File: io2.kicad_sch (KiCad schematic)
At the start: 59 parts, among them IC1 ILD217T, IC2 ILD217T, Q10 BC846, Q11 BC846, Q8 BC846, Q9 BC846, U11 74HC14, U12 74HC165, X3 Conn_DI

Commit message: Redesign PCB
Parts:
- added C13, C14: 100n, Capacitor_SMD:C_0603_1608Metric, symbol Device:C_Small
- added C29: 22µ, Capacitor_SMD:CP_Elec_4x5.8, symbol Device:C_Polarized_Small
- added JP5: DI_VCC, Jumper:SolderJumper-2_P1.3mm_Open_RoundedPad1.0x1.5mm, symbol Jumper:SolderJumper_2_Open
- added JP6: DI_GND, Jumper:SolderJumper-2_P1.3mm_Open_RoundedPad1.0x1.5mm, symbol Jumper:SolderJumper_2_Open
- added PS2: TEA 1-0505, Converter_DCDC:Converter_DCDC_Murata_MEE1SxxxxSC_THT, symbol Converter_DCDC:MEE1S0303SC
- added R56: n.b., Resistor_SMD:R_0603_1608Metric, symbol Device:R_Small
- D20, D21, D22, D23: footprint Package_TO_SOT_SMD:SOT-323_SC-70 -> Package_TO_SOT_SMD:SOT-23
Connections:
- net +3V3: now also U12.4 (D5)
- net +5V: now also C13.1, JP5.1 (A), PS2.2 (+Vin); no longer X3.5 (Pin_5), X3.6 (Pin_6)
- net DI2_P: now also X3.3 (Pin_3); no longer X3.2 (Pin_2)
- net DI3_P: now also X3.5 (Pin_5); no longer X3.3 (Pin_3)
- net DI4_P: now also X3.7 (Pin_7); no longer X3.4 (Pin_4)
- net GND: now also C13.2, JP6.1 (A), PS2.1 (-Vin); no longer U12.4 (D5), X3.8 (Pin_8), X3.9 (Pin_9)
- net GND1: now also X3.9 (Pin_9), C14.2, C29.2, JP6.2 (B), PS2.3 (-Vout), R56.1; no longer X3.7 (Pin_7)
- new net 5V_1: C14.1, C29.1, JP5.2 (B), PS2.4 (+Vout), R56.2, X3.2 (Pin_2), X3.4 (Pin_4), X3.6 (Pin_6), X3.8 (Pin_8)
- no-connect marks 1 -> 3
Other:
- note added: "Alternativbestückung: PS2 oder JP5,JP6"
- note added: "HW0"
- note added: "HW1"
- note added: "HW2"
- note added: "Reserve"
- note removed: "ToDo: BAT54 falscher Footprint"
- moved on the sheet: C27, U11E, U11F, U11G, X3

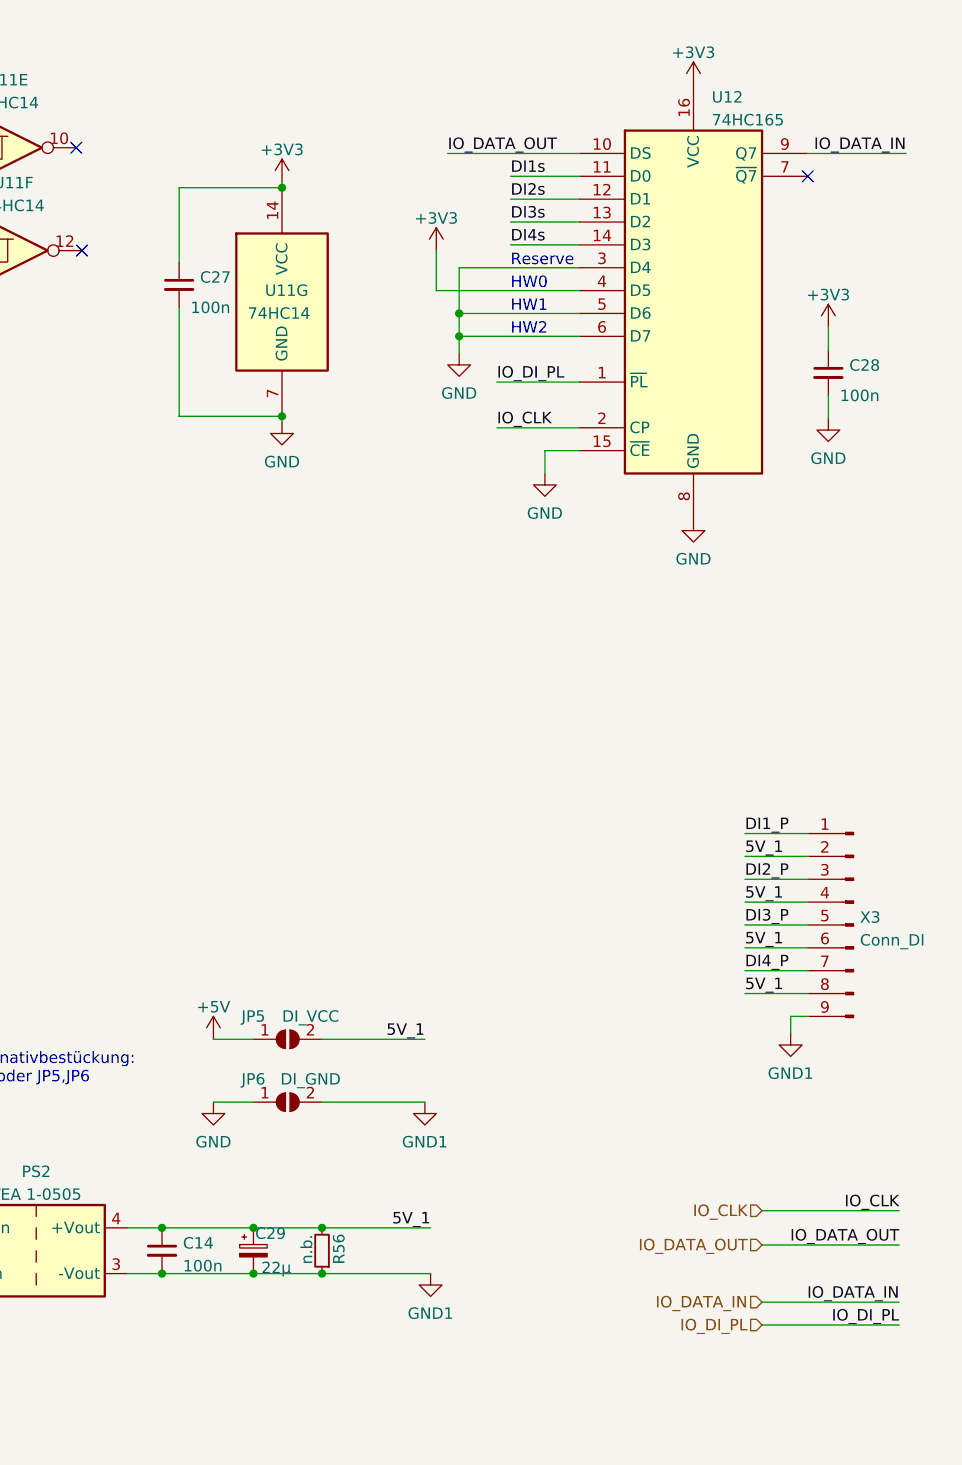
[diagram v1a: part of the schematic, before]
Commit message: Layout optimized
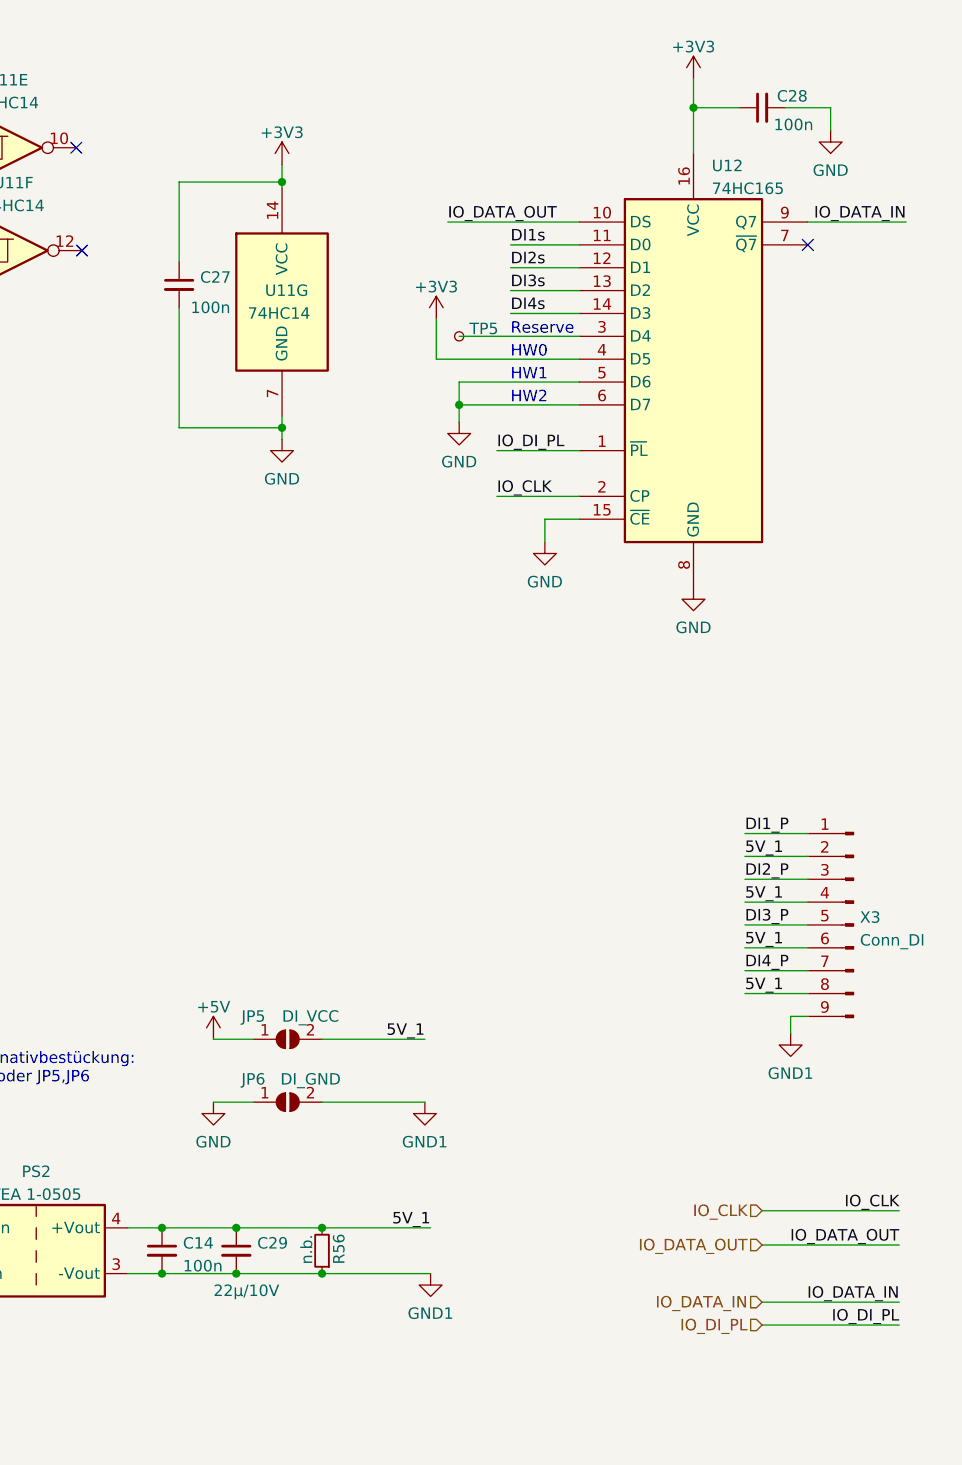
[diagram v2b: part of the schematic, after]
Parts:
- removed C29: 22µ, Capacitor_SMD:CP_Elec_4x5.8, symbol Device:C_Polarized_Small
- added C29: 22µ/10V, Capacitor_SMD:C_1206_3216Metric, symbol Device:C_Small
- added TP5: TP, TestPoint:TestPoint_Pad_1.0x1.0mm, symbol Connector:TestPoint_Small
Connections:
- net 5V_1: now also C29.1
- net GND: no longer U12.3 (D4)
- net GND1: now also C29.2
- new net: TP5.1, U12.3 (D4)
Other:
- moved on the sheet: C28, U12

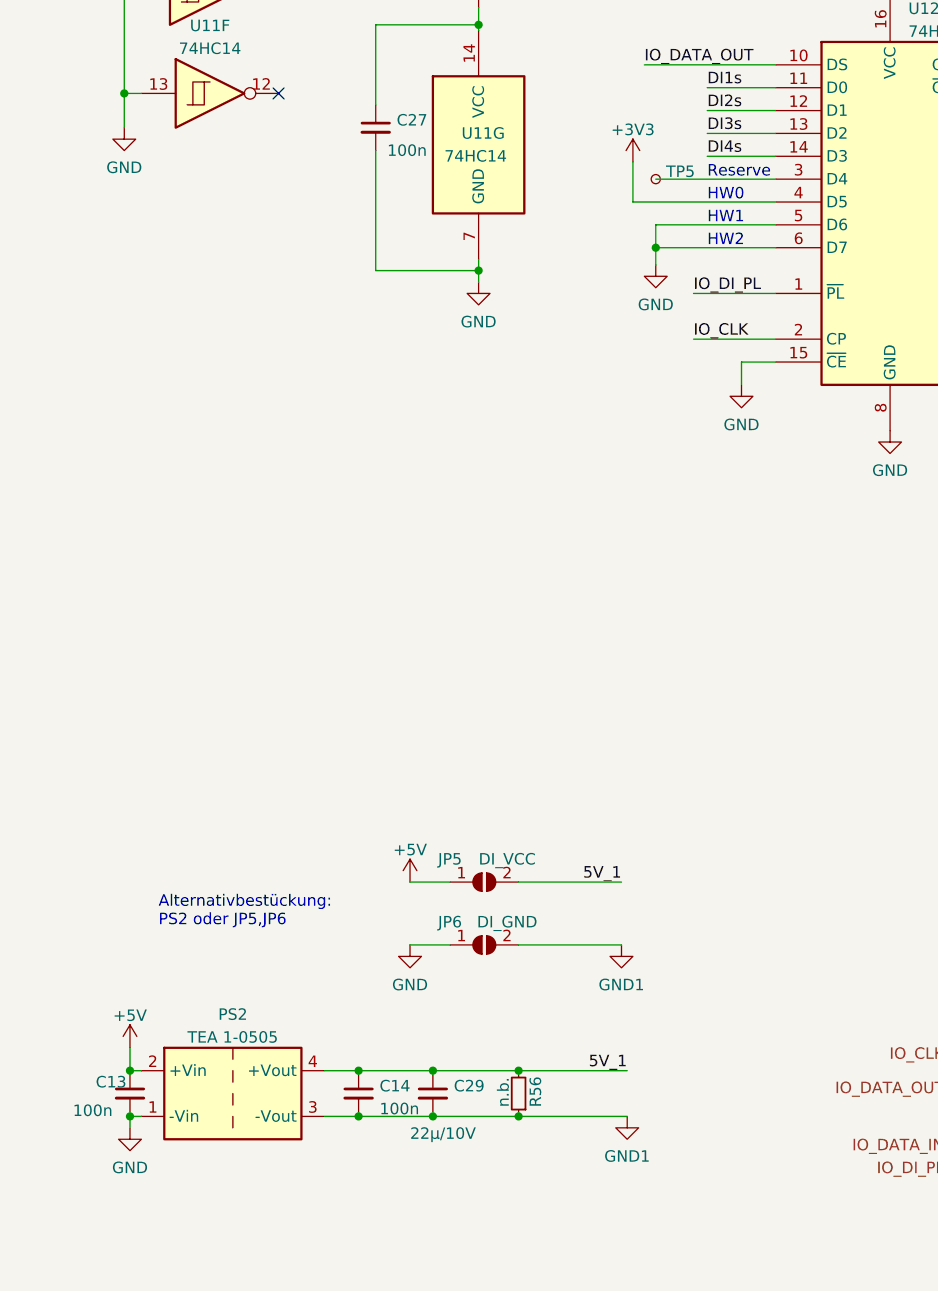
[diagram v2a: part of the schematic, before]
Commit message: Change extension bus
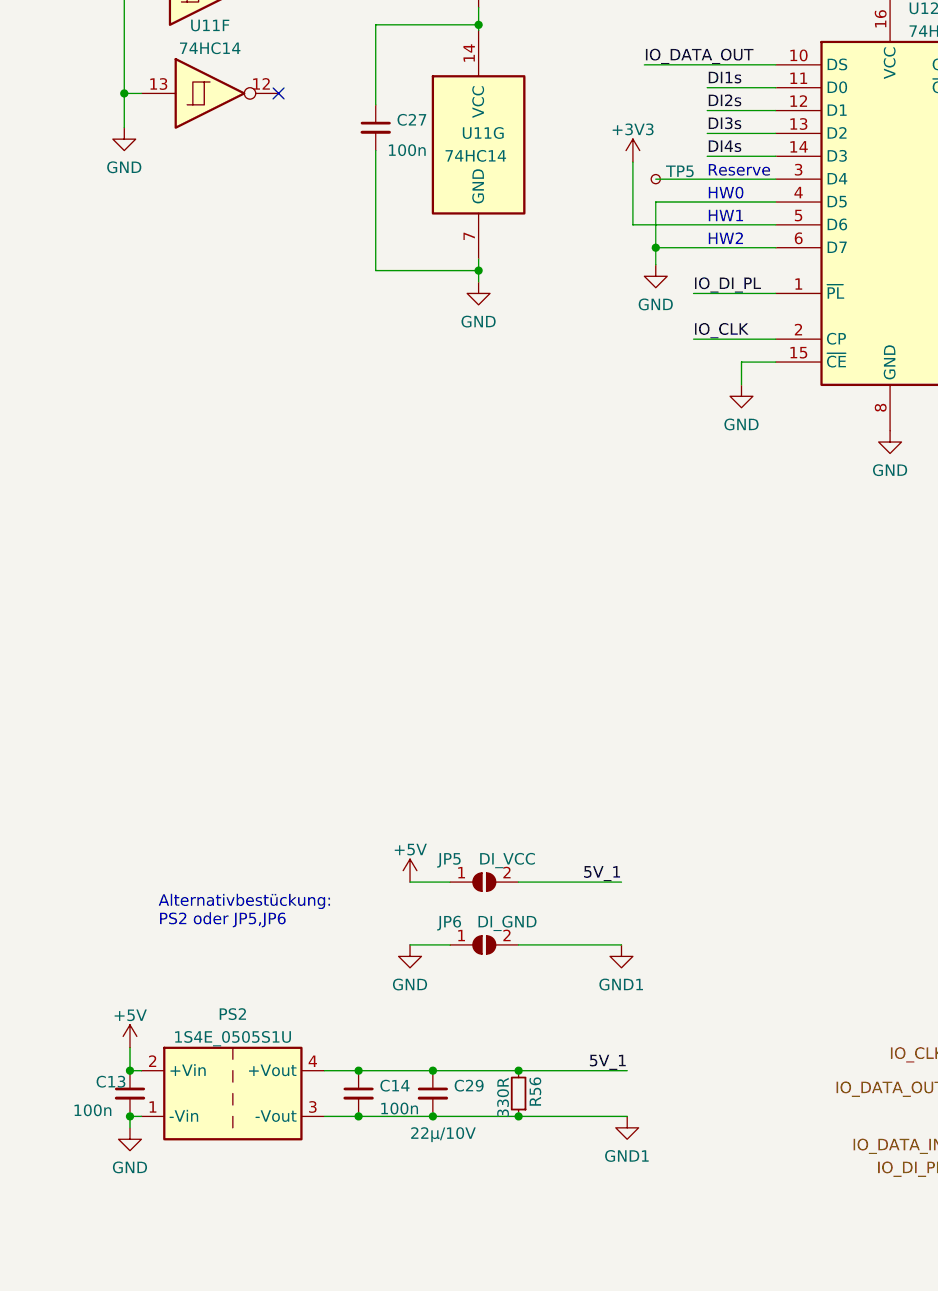
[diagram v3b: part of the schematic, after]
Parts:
- D20, D21, D22, D23: footprint Package_TO_SOT_SMD:SOT-23 -> Package_TO_SOT_SMD:SOT-323_SC-70
- IC1, IC2: footprint Package_SO:SOIC-8_5.23x5.23mm_P1.27mm -> Package_SO:SOIC-8_3.9x4.9mm_P1.27mm
- PS2: value TEA 1-0505 -> 1S4E_0505S1U; footprint Converter_DCDC:Converter_DCDC_Murata_MEE1SxxxxSC_THT -> custom_th:Converter_DCDC_GAPTEC_1S4E_S1U
- R56: value n.b. -> 330R
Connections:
- net +3V3: now also U12.5 (D6); no longer U12.4 (D5)
- net GND: now also U12.4 (D5); no longer U12.5 (D6)
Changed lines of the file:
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@@
   (title_block
     (title "BSC")
-    (date "2022-12-16")
-    (rev "2.1")
+    (date "2023-03-30")
+    (rev "2.3")
   )
   (junction (at 115.57 118.745) (diameter 0) (color 0 0 0 0)
@@
     (stroke (width 0) (type default) (color 0 0 0 0))
   )
-  (wire (pts (xy 227.33 48.26) (xy 227.33 52.705))
+  (wire (pts (xy 227.33 48.26) (xy 227.33 55.245))
     (stroke (width 0) (type default) (color 0 0 0 0))
   )
@@
     (stroke (width 0) (type default) (color 0 0 0 0))
   )
-  (wire (pts (xy 229.87 55.245) (xy 243.205 55.245))
-    (stroke (width 0) (type default) (color 0 0 0 0))
-  )
   (wire (pts (xy 145.415 132.08) (xy 151.765 132.08))
     (stroke (width 0) (type default) (color 0 0 0 0))
@@
     (stroke (width 0) (type default) (color 0 0 0 0))
   )
+  (wire (pts (xy 227.33 55.245) (xy 243.205 55.245))
+    (stroke (width 0) (type default) (color 0 0 0 0))
+  )
   (wire (pts (xy 93.345 29.21) (xy 95.885 29.21))
     (stroke (width 0) (type default) (color 0 0 0 0))
@@
     (stroke (width 0) (type default) (color 0 0 0 0))
   )
+  (wire (pts (xy 229.87 52.705) (xy 243.205 52.705))
+    (stroke (width 0) (type default) (color 0 0 0 0))
+  )
   (wire (pts (xy 67.945 118.745) (xy 65.405 118.745))
     (stroke (width 0) (type default) (color 0 0 0 0))
@@
     (stroke (width 0) (type default) (color 0 0 0 0))
   )
-  (wire (pts (xy 229.87 55.245) (xy 229.87 57.785))
+  (wire (pts (xy 229.87 52.705) (xy 229.87 57.785))
     (stroke (width 0) (type default) (color 0 0 0 0))
   )
@@
   )
   (wire (pts (xy 263.525 157.48) (xy 278.765 157.48))
-    (stroke (width 0) (type default) (color 0 0 0 0))
-  )
-  (wire (pts (xy 227.33 52.705) (xy 243.205 52.705))
     (stroke (width 0) (type default) (color 0 0 0 0))
   )
@@
       (effects (font (size 1.27 1.27)) (justify left))
     )
-    (property "Footprint" "Package_TO_SOT_SMD:SOT-23" (id 2) (at 22.225 34.29 0)
+    (property "Footprint" "Package_TO_SOT_SMD:SOT-323_SC-70" (id 2) (at 22.225 34.29 0)
       (effects (font (size 1.27 1.27)) hide)
     )
@@
       (effects (font (size 1.27 1.27)) (justify left))
     )
-    (property "Footprint" "Package_TO_SOT_SMD:SOT-23" (id 2) (at 22.225 162.56 0)
+    (property "Footprint" "Package_TO_SOT_SMD:SOT-323_SC-70" (id 2) (at 22.225 162.56 0)
       (effects (font (size 1.27 1.27)) hide)
     )
@@
       (effects (font (size 1.27 1.27)) (justify left))
     )
-    (property "Value" "n.b." (id 1) (at 212.9463 149.9606 90)
+    (property "Value" "330R" (id 1) (at 212.9463 149.9606 90)
       (effects (font (size 1.27 1.27)) (justify left))
     )
@@
       (effects (font (size 1.27 1.27)) (justify left))
     )
-    (property "Footprint" "Package_TO_SOT_SMD:SOT-23" (id 2) (at 22.225 73.025 0)
+    (property "Footprint" "Package_TO_SOT_SMD:SOT-323_SC-70" (id 2) (at 22.225 73.025 0)
       (effects (font (size 1.27 1.27)) hide)
     )
@@
     (property "Reference" "IC2" (id 0) (at 80.645 112.556 0))
     (property "Value" "ILD217T" (id 1) (at 80.645 115.0929 0))
-    (property "Footprint" "Package_SO:SOIC-8_5.23x5.23mm_P1.27mm" (id 2) (at 89.535 116.205 0)
+    (property "Footprint" "Package_SO:SOIC-8_3.9x4.9mm_P1.27mm" (id 2) (at 89.535 116.205 0)
       (effects (font (size 1.27 1.27)) (justify left) hide)
     )
@@
     (in_bom yes) (on_board yes) (fields_autoplaced)
     (property "Reference" "PS2" (id 0) (at 182.88 142.9852 0))
-    (property "Value" "TEA 1-0505" (id 1) (at 182.88 145.5221 0))
-    (property "Footprint" "Converter_DCDC:Converter_DCDC_Murata_MEE1SxxxxSC_THT" (id 2) (at 156.21 158.115 0)
+    (property "Value" "1S4E_0505S1U" (id 1) (at 182.88 145.5221 0))
+    (property "Footprint" "custom_th:Converter_DCDC_GAPTEC_1S4E_S1U" (id 2) (at 156.21 158.115 0)
       (effects (font (size 1.27 1.27)) (justify left) hide)
     )
@@
       (effects (font (size 1.27 1.27)) (justify left))
     )
-    (property "Footprint" "Package_TO_SOT_SMD:SOT-23" (id 2) (at 22.225 123.825 0)
+    (property "Footprint" "Package_TO_SOT_SMD:SOT-323_SC-70" (id 2) (at 22.225 123.825 0)
       (effects (font (size 1.27 1.27)) hide)
     )
@@
     (property "Reference" "IC1" (id 0) (at 80.645 23.021 0))
     (property "Value" "ILD217T" (id 1) (at 80.645 25.5579 0))
-    (property "Footprint" "Package_SO:SOIC-8_5.23x5.23mm_P1.27mm" (id 2) (at 89.535 26.67 0)
+    (property "Footprint" "Package_SO:SOIC-8_3.9x4.9mm_P1.27mm" (id 2) (at 89.535 26.67 0)
       (effects (font (size 1.27 1.27)) (justify left) hide)
     )
